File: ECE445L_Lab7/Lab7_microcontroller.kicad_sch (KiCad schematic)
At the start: 1 part, among them U1 EK-TM4C123GXL

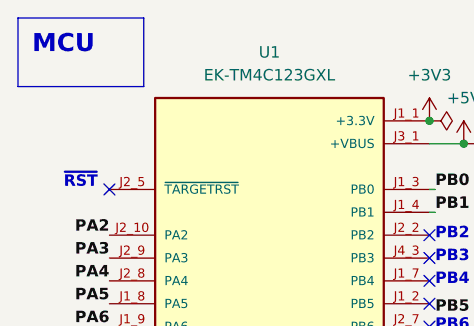
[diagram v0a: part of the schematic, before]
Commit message: update all symbols and re-sync footprints in the KiCad projects
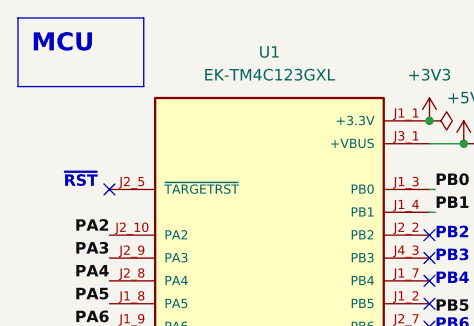
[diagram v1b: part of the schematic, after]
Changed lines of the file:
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@@
 (kicad_sch
-	(version 20231120)
+	(version 20250114)
 	(generator "eeschema")
-	(generator_version "8.0")
+	(generator_version "9.0")
 	(paper "A4")
+	(text "~{RST}"
+		(exclude_from_sim no)
+		(at 48.26 59.055 0)
+		(effects
+			(font
+				(size 1.27 1.27)
+				(bold yes)
+			)
+			(justify left bottom)
+		)
+	)
+	(text "PB2"
+		(exclude_from_sim no)
+		(at 89.535 64.77 0)
+		(effects
+			(font
+				(size 1.27 1.27)
+				(bold yes)
+			)
+			(justify left bottom)
+		)
+	)
+	(text "PD3"
+		(exclude_from_sim no)
+		(at 89.535 90.17 0)
+		(effects
+			(font
+				(size 1.27 1.27)
+				(bold yes)
+			)
+			(justify left bottom)
+		)
+	)
+	(text "PF3"
+		(exclude_from_sim no)
+		(at 90.17 107.315 0)
+		(effects
+			(font
+				(size 1.27 1.27)
+				(bold yes)
+			)
+			(justify left bottom)
+		)
+	)
+	(text "PB3"
+		(exclude_from_sim no)
+		(at 89.535 67.31 0)
+		(effects
+			(font
+				(size 1.27 1.27)
+				(bold yes)
+			)
+			(justify left bottom)
+		)
+	)
+	(text "PB4"
+		(exclude_from_sim no)
+		(at 89.535 69.85 0)
+		(effects
+			(font
+				(size 1.27 1.27)
+				(bold yes)
+			)
+			(justify left bottom)
+		)
+	)
+	(text "PD1"
+		(exclude_from_sim no)
+		(at 89.535 85.09 0)
+		(effects
+			(font
+				(size 1.27 1.27)
+				(bold yes)
+			)
+			(justify left bottom)
+		)
+	)
+	(text "PF1"
+		(exclude_from_sim no)
+		(at 90.17 102.235 0)
+		(effects
+			(font
+				(size 1.27 1.27)
+				(bold yes)
+			)
+			(justify left bottom)
+		)
+	)
+	(text "PB6"
+		(exclude_from_sim no)
+		(at 89.535 74.93 0)
+		(effects
+			(font
+				(size 1.27 1.27)
+				(bold yes)
+			)
+			(justify left bottom)
+		)
+	)
+	(text "PD0"
+		(exclude_from_sim no)
+		(at 89.535 82.55 0)
+		(effects
+			(font
+				(size 1.27 1.27)
+				(bold yes)
+			)
+			(justify left bottom)
+		)
+	)
+	(text "PF2"
+		(exclude_from_sim no)
+		(at 90.17 104.775 0)
+		(effects
+			(font
+				(size 1.27 1.27)
+				(bold yes)
+			)
+			(justify left bottom)
+		)
+	)
+	(text "PF0"
+		(exclude_from_sim no)
+		(at 90.17 99.695 0)
+		(effects
+			(font
+				(size 1.27 1.27)
+				(bold yes)
+			)
+			(justify left bottom)
+		)
+	)
+	(text_box "MCU"
+		(exclude_from_sim no)
+		(at 43.18 40.005 0)
+		(size 13.97 7.62)
+		(margins 1.5 1.5 1.5 1.5)
+		(stroke
+			(width 0)
+			(type default)
+		)
+		(fill
+			(type none)
+		)
+		(effects
+			(font
+				(size 2 2)
+				(thickness 0.4)
+				(bold yes)
+			)
+			(justify left top)
+		)
+	)
 	(junction
 		(at 88.9 51.435)
@@
 		)
 	)
-	(text_box "MCU"
-		(exclude_from_sim no)
-		(at 43.18 40.005 0)
-		(size 13.97 7.62)
-		(stroke
-			(width 0)
-			(type default)
-		)
-		(fill
-			(type none)
-		)
-		(effects
-			(font
-				(size 2 2)
-				(thickness 0.4)
-				(bold yes)
-			)
-			(justify left top)
-		)
-	)
-	(text "~{RST}"
-		(exclude_from_sim no)
-		(at 48.26 59.055 0)
-		(effects
-			(font
-				(size 1.27 1.27)
-				(bold yes)
-			)
-			(justify left bottom)
-		)
-	)
-	(text "PB2"
-		(exclude_from_sim no)
-		(at 89.535 64.77 0)
-		(effects
-			(font
-				(size 1.27 1.27)
-				(bold yes)
-			)
-			(justify left bottom)
-		)
-	)
-	(text "PD3"
-		(exclude_from_sim no)
-		(at 89.535 90.17 0)
-		(effects
-			(font
-				(size 1.27 1.27)
-				(bold yes)
-			)
-			(justify left bottom)
-		)
-	)
-	(text "PF3"
-		(exclude_from_sim no)
-		(at 90.17 107.315 0)
-		(effects
-			(font
-				(size 1.27 1.27)
-				(bold yes)
-			)
-			(justify left bottom)
-		)
-	)
-	(text "PB3"
-		(exclude_from_sim no)
-		(at 89.535 67.31 0)
-		(effects
-			(font
-				(size 1.27 1.27)
-				(bold yes)
-			)
-			(justify left bottom)
-		)
-	)
-	(text "PB4"
-		(exclude_from_sim no)
-		(at 89.535 69.85 0)
-		(effects
-			(font
-				(size 1.27 1.27)
-				(bold yes)
-			)
-			(justify left bottom)
-		)
-	)
-	(text "PD1"
-		(exclude_from_sim no)
-		(at 89.535 85.09 0)
-		(effects
-			(font
-				(size 1.27 1.27)
-				(bold yes)
-			)
-			(justify left bottom)
-		)
-	)
-	(text "PF1"
-		(exclude_from_sim no)
-		(at 90.17 102.235 0)
-		(effects
-			(font
-				(size 1.27 1.27)
-				(bold yes)
-			)
-			(justify left bottom)
-		)
-	)
-	(text "PB6"
-		(exclude_from_sim no)
-		(at 89.535 74.93 0)
-		(effects
-			(font
-				(size 1.27 1.27)
-				(bold yes)
-			)
-			(justify left bottom)
-		)
-	)
-	(text "PD0"
-		(exclude_from_sim no)
-		(at 89.535 82.55 0)
-		(effects
-			(font
-				(size 1.27 1.27)
-				(bold yes)
-			)
-			(justify left bottom)
-		)
-	)
-	(text "PF2"
-		(exclude_from_sim no)
-		(at 90.17 104.775 0)
-		(effects
-			(font
-				(size 1.27 1.27)
-				(bold yes)
-			)
-			(justify left bottom)
-		)
-	)
-	(text "PF0"
-		(exclude_from_sim no)
-		(at 90.17 99.695 0)
-		(effects
-			(font
-				(size 1.27 1.27)
-				(bold yes)
-			)
-			(justify left bottom)
-		)
-	)
 	(label "PE2"
 		(at 48.895 99.695 0)
-		(fields_autoplaced yes)
 		(effects
 			(font
@@
 	(label "PA7"
 		(at 53.34 76.835 180)
-		(fields_autoplaced yes)
 		(effects
 			(font
@@
 	(label "PD6"
 		(at 89.535 92.71 0)
-		(fields_autoplaced yes)
 		(effects
 			(font
@@
 	(label "PC5"
 		(at 53.34 84.455 180)
-		(fields_autoplaced yes)
 		(effects
 			(font
@@
 	(label "PB1"
 		(at 89.535 61.595 0)
-		(fields_autoplaced yes)
 		(effects
 			(font
@@
 	(label "PC6"
 		(at 53.34 86.995 180)
-		(fields_autoplaced yes)
 		(effects
 			(font
@@
 	(label "PB7"
 		(at 89.535 78.105 0)
-		(fields_autoplaced yes)
 		(effects
 			(font
@@
 	(label "PA2"
 		(at 53.34 64.135 180)
-		(fields_autoplaced yes)
 		(effects
 			(font
@@
 	(label "PA4"
 		(at 53.34 69.215 180)
-		(fields_autoplaced yes)
 		(effects
 			(font
@@
 	(label "PC4"
 		(at 53.34 81.915 180)
-		(fields_autoplaced yes)
 		(effects
 			(font
@@
 	(label "PB5"
 		(at 89.535 73.025 0)
-		(fields_autoplaced yes)
 		(effects
 			(font
@@
 	(label "PD7"
 		(at 89.535 95.25 0)
-		(fields_autoplaced yes)
 		(effects
 			(font
@@
 	(label "PA3"
 		(at 53.34 66.675 180)
-		(fields_autoplaced yes)
 		(effects
 			(font
@@
 	(label "PF4"
 		(at 88.9 109.855 0)
-		(fields_autoplaced yes)
 		(effects
 			(font
@@
 	(label "PE4"
 		(at 53.34 104.775 180)
-		(fields_autoplaced yes)
 		(effects
 			(font
@@
 	(label "PD2"
 		(at 89.535 87.63 0)
-		(fields_autoplaced yes)
 		(effects
 			(font
@@
 	(label "PA5"
 		(at 53.34 71.755 180)
-		(fields_autoplaced yes)
 		(effects
 			(font
@@
 	(label "PE0"
 		(at 53.34 94.615 180)
-		(fields_autoplaced yes)
 		(effects
 			(font
@@
 	(label "PC7"
 		(at 53.34 89.535 180)
-		(fields_autoplaced yes)
 		(effects
 			(font
@@
 	(label "PE5"
 		(at 53.34 107.315 180)
-		(fields_autoplaced yes)
 		(effects
 			(font
@@
 	(label "PE1"
 		(at 53.34 97.155 180)
-		(fields_autoplaced yes)
 		(effects
 			(font
@@
 	(label "PB0"
 		(at 89.535 59.055 0)
-		(fields_autoplaced yes)
 		(effects
 			(font
@@
 	(label "PE3"
 		(at 48.895 102.235 0)
-		(fields_autoplaced yes)
 		(effects
 			(font
@@
 	(label "PA6"
 		(at 53.34 74.295 180)
-		(fields_autoplaced yes)
-		(effects
-			(font
+		(effects
+			(font
